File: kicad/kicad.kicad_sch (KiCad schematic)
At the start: 2 parts, among them U1 AS6C1616, U2 AS6C1616

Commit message: Add concat
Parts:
- removed U1, U2: AS6C1616, Package_SO:TSOP-I-48_18.4x12mm_P0.5mm, symbol Memory_RAM:AS6C1616
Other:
- added sheet SRAM Depth Concat (sram_depth_concat.kicad_sch)
- added sheet SRAM Width Concat (sram_width_concat.kicad_sch)

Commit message: Add sdram calibration WIP
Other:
- added sheet SDRAM (sdram.kicad_sch)
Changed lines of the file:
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@@
 (kicad_sch (version 20230121) (generator eeschema)
   (paper "A4")
+  (sheet (at 27.94 54.61) (size 24.13 8.89) (fields_autoplaced)
+    (stroke (width 0.1524) (type solid) (color 132 0 132 1))
+    (fill (color 255 255 255 0.0000))
+    (property "Sheetname" "SDRAM" (at 27.94 53.8984 0)
+      (effects (font (size 1.27 1.27)) (justify left bottom))
+    )
+    (property "Sheetfile" "sdram.kicad_sch" (at 27.94 64.0846 0)
+      (effects (font (size 1.27 1.27)) (justify left top))
+    )
+    (instances
+      (project "kicad"
+        (path "/5861ef52-8816-4dbf-b79a-8738bf9b392b" (page "4"))
+      )
+    )
+  )
   (sheet (at 27.94 24.13) (size 24.13 8.89) (fields_autoplaced)
     (stroke (width 0.1524) (type solid) (color 132 0 132 1))

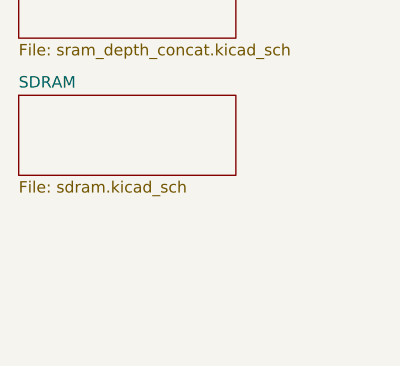
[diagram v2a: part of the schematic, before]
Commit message: Add initial sdram en
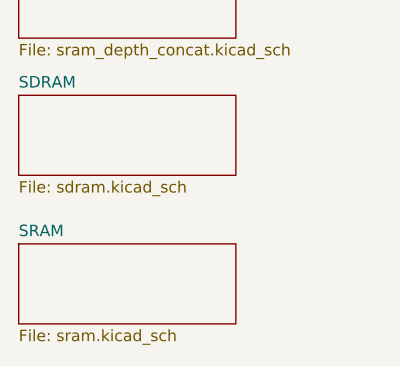
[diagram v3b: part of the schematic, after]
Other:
- added sheet SRAM (sram.kicad_sch)
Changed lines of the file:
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@@
+    )
+  )
+  (sheet (at 27.94 71.12) (size 24.13 8.89) (fields_autoplaced)
+    (stroke (width 0.1524) (type solid) (color 132 0 132 1))
+    (fill (color 255 255 255 0.0000))
+    (property "Sheetname" "SRAM" (at 27.94 70.4084 0)
+      (effects (font (size 1.27 1.27)) (justify left bottom))
+    )
+    (property "Sheetfile" "sram.kicad_sch" (at 27.94 80.5946 0)
+      (effects (font (size 1.27 1.27)) (justify left top))
+    )
+    (instances
+      (project "kicad"
+        (path "/5861ef52-8816-4dbf-b79a-8738bf9b392b" (page "5"))
+      )
     )
   )
